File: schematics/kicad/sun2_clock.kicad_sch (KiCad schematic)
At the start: 7 parts, among them U102 74F00, U200 20Mhz, U201 74F74, U203 74F74, U204 74F74, U205 74F74, U313 74F08

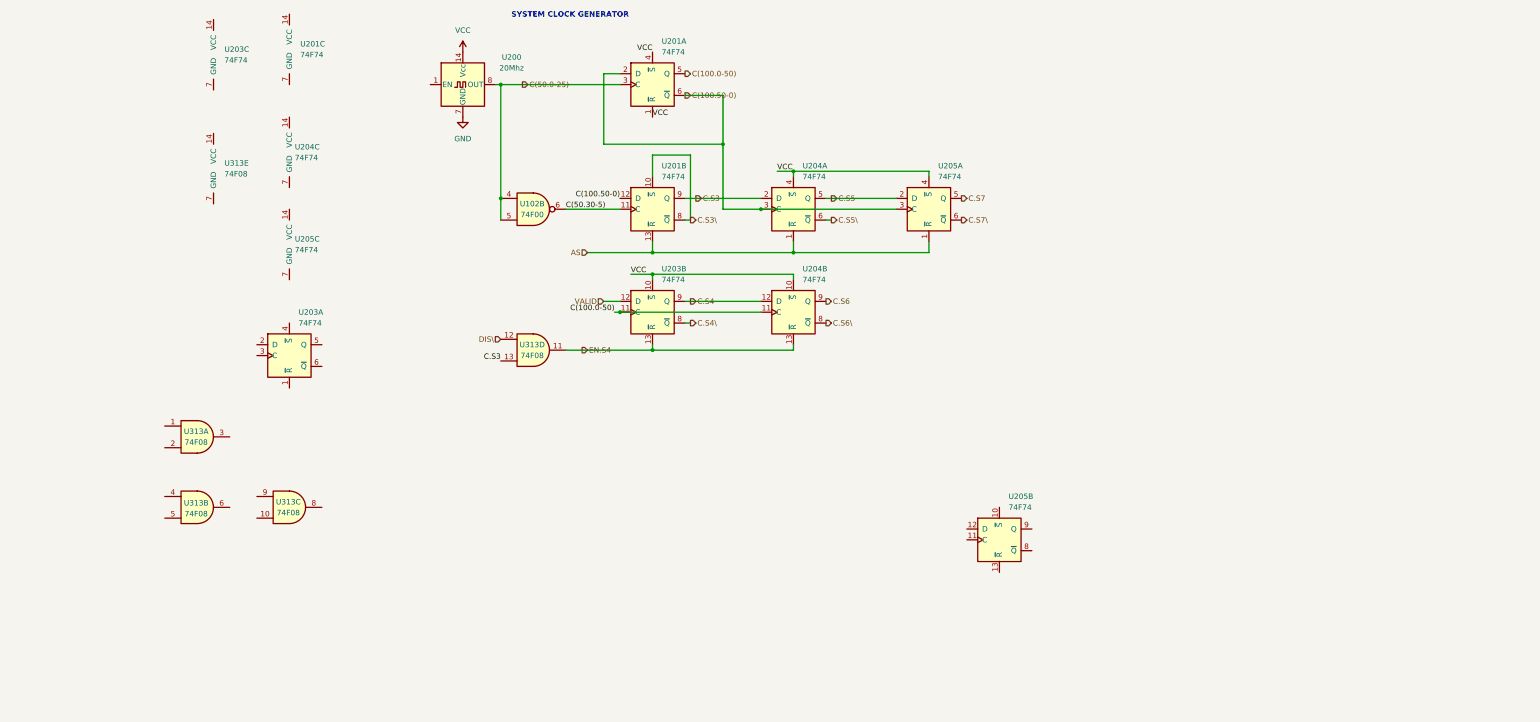
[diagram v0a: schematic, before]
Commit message: Finish page2: Clock, Timers, DVMA
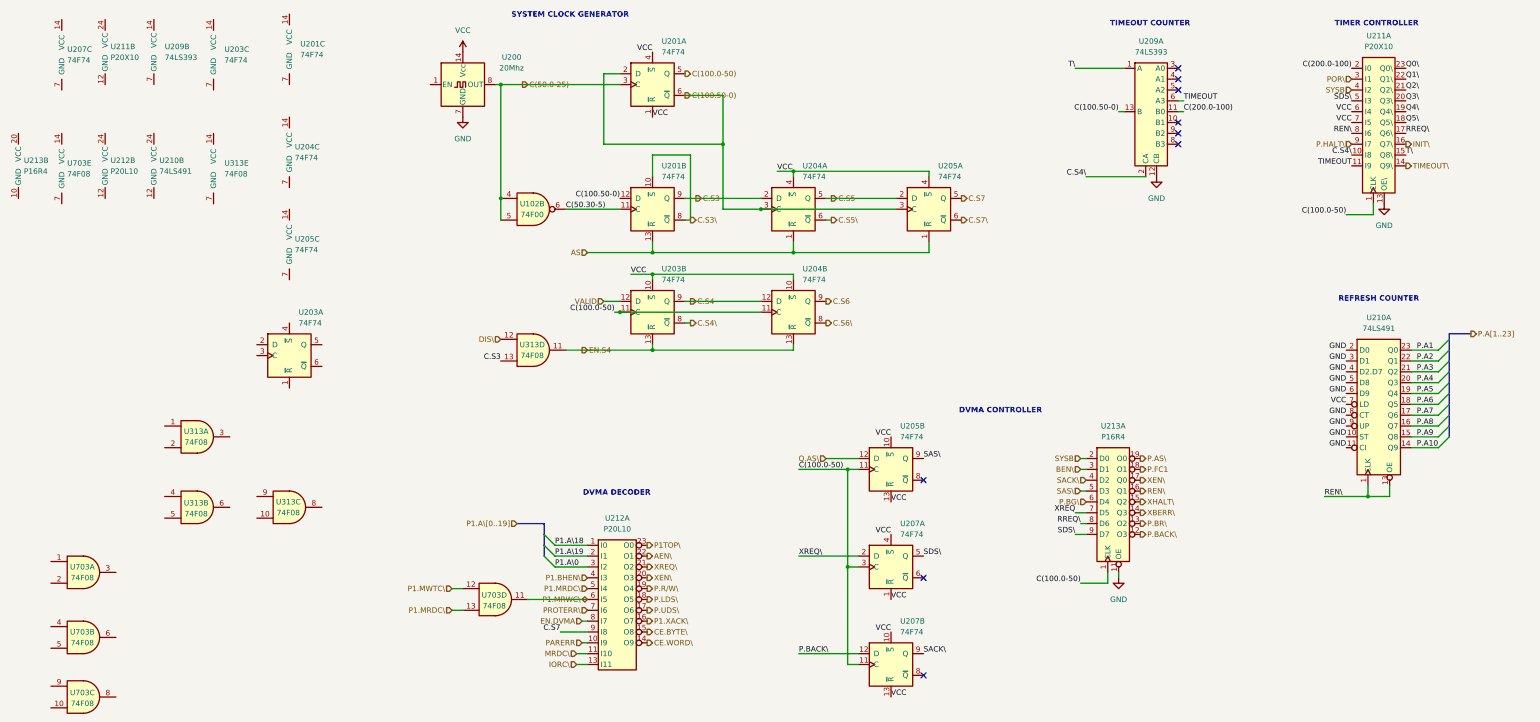
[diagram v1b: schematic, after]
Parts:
- added U207: 74F74, Package_DIP:DIP-14_W7.62mm, symbol sun2:74F74
- added U209: 74LS393, Package_DIP:DIP-14_W7.62mm, symbol sun2:74LS393
- added U210: 74LS491, Package_DIP:DIP-24_W7.62mm, symbol sun2:74LS491
- added U211: P20X10, Package_DIP:DIP-24_W7.62mm, symbol sun2:P20X10
- added U212: P20L10, Package_DIP:DIP-24_W7.62mm, symbol sun2:P20L10
- added U213: P16R4, Package_DIP:DIP-20_W7.62mm, symbol sun2:P16R4
- added U703: 74F08, Package_DIP:DIP-14_W7.62mm, symbol sun2:74F08
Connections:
- net C(100.0-50): now also U205.11 (C), U207.11 (C), U207.3 (C), U211.1 (CLK), U213.1 (CLK)
- net C(100.50-0): now also U209.13 (B)
- net C.S4\: now also U209.2 (CA), U211.10 (I8)
- net C.S7: now also U212.9 (I8)
- net GND: now also U209.12 (CB), U210.10 (ST), U210.11 (CI), U210.2 (D0), U210.3 (D1), U210.4 (D2.D7), U210.5 (D8), U210.6 (D9), U210.8 (CT), U210.9 (UP), U211.13 (OE\), U213.11 (OE)
- net VCC: now also U205.10 (~{S}), U205.13 (~{R}), U207.1 (~{R}), U207.10 (~{S}), U207.13 (~{R}), U207.4 (~{S}), U210.7 (LD), U211.6 (I4), U211.7 (I5)
- net Q.AS\: now reaches U205.12 (D)
- net SAS\: now reaches U205.9 (Q)
- net SAS\: now also U213.5 (D3)
- new net AEN\: U212.22 (O1)
- new net BEN\: U213.3 (D1)
- new net C(200.0-100): U209.11 (B0), U211.2 (I0)
- new net CE.BYTE\: U212.15 (O8)
- new net CE.WORD\: U212.14 (O9)
- new net EN.DVMA: U212.8 (I7)
- new net INIT\: U211.16 (Q7\)
- new net IORC\: U212.13 (I11)
- new net MRDC\: U212.11 (I10)
- new net P.A1: U210.23 (Q0)
- new net P.A10: U210.14 (Q9)
- new net P.A2: U210.22 (Q1)
- new net P.A3: U210.21 (Q2)
- new net P.A4: U210.20 (Q3)
- new net P.A5: U210.19 (Q4)
- new net P.A6: U210.18 (Q5)
- new net P.A7: U210.17 (Q6)
- new net P.A8: U210.16 (Q7)
- new net P.A9: U210.15 (Q8)
- new net P.AS\: U213.19 (O0)
- new net P.BACK\: U207.12 (D), U213.12 (O3)
- new net P.BG\: U213.6 (D4)
- new net P.BR\: U213.13 (O2)
- new net P.FC1: U213.18 (O1)
- new net P.HALT\: U211.9 (I7)
- new net P.LDS\: U212.18 (O5)
- new net P.R/W\: U212.19 (O4)
- new net P.UDS\: U212.17 (O6)
- new net P1.A\0: U212.3 (I2)
- new net P1.A\18: U212.1 (I0)
- new net P1.A\19: U212.2 (I1)
- new net P1.BHEN\: U212.4 (I3)
- new net P1.MRDC\: U212.5 (I4), U703.13
- new net P1.MRWC\: U212.6 (I5), U703.11
- new net P1.MWTC\: U703.12
- new net P1.XACK\: U212.16 (O7)
- new net P1TOP\: U212.23 (O0)
- new net PARERR: U212.10 (I9)
- new net POR\: U211.3 (I1)
- new net PROTERR\: U212.7 (I6)
- new net Q0\: U211.23 (Q0\)
- new net Q1\: U211.22 (Q1\)
- new net Q2\: U211.21 (Q2\)
- new net Q3\: U211.20 (Q3\)
- new net Q4\: U211.19 (Q4\)
- new net Q5\: U211.18 (Q5\)
- new net REN\: U210.1 (CLK), U210.13 (OE), U211.8 (I6), U213.16 (Q1)
- new net RREQ\: U211.17 (Q6\), U213.8 (D6)
- new net SACK\: U207.9 (Q), U213.4 (D2)
- new net SDS\: U207.5 (Q), U211.5 (I3), U213.9 (D7)
- new net SYSB: U211.4 (I2), U213.2 (D0)
- new net TIMEOUT: U209.6 (A3), U211.11 (I9)
- new net TIMEOUT\: U211.14 (Q9\)
- new net T\: U209.1 (A), U211.15 (Q8\)
- new net XBERR\: U213.14 (Q3)
- new net XEN\: U212.20 (O3), U213.17 (Q0)
- new net XHALT\: U213.15 (Q2)
- new net XREQ: U213.7 (D5)
- new net XREQ\: U207.2 (D), U212.21 (O2)
- no-connect marks 0 -> 9
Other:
- note added: "DVMA CONTROLLER"
- note added: "DVMA DECODER"
- note added: "REFRESH COUNTER"
- note added: "TIMEOUT COUNTER"
- note added: "TIMER CONTROLLER"
- moved on the sheet: U205B

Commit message: more mmu work
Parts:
- removed unit 2 of U210
- removed unit 2 of U212
- removed unit 2 of U213
- removed unit 1 of U313
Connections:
- net GND: now also U210.12 (GND), U212.12 (GND), U213.10 (GND)
- net VCC: now also U210.24 (VCC), U212.24 (VCC), U213.20 (VCC)
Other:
- moved on the sheet: U209A, U211A

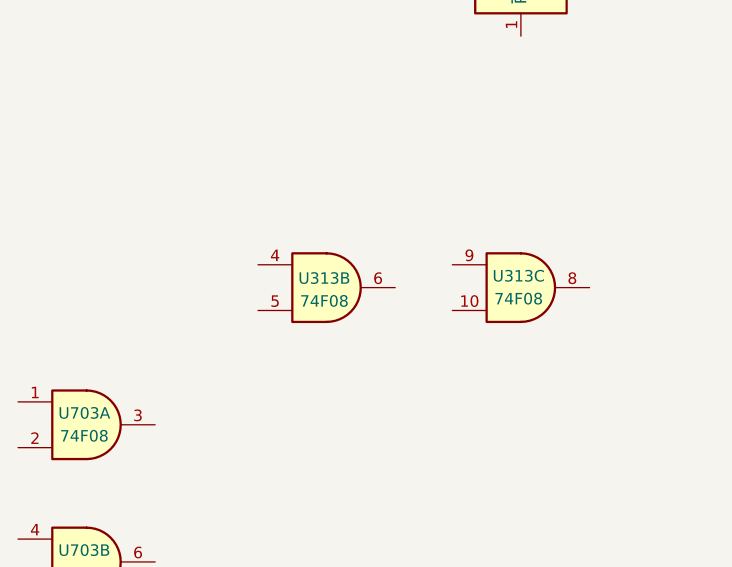
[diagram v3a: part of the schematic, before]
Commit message: Start on rasterop, parity, P2
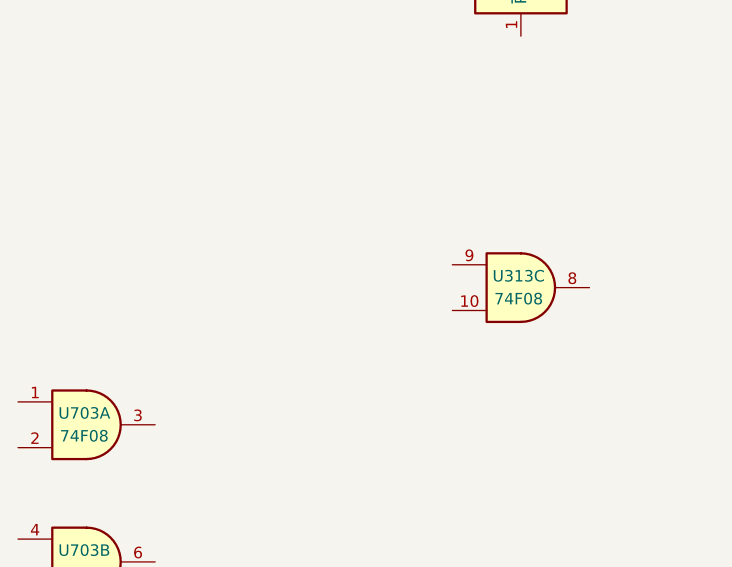
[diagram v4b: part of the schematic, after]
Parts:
- removed unit 2 of U313
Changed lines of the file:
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@@
-	)
-	(symbol
-		(lib_id "sun2:74F08")
-		(at -31.75 135.89 0)
-		(unit 2)
-		(exclude_from_sim no)
-		(in_bom yes)
-		(on_board yes)
-		(dnp no)
-		(property "Reference" "U313"
-			(at -32.004 134.874 0)
-			(effects
-				(font
-					(size 1.27 1.27)
-				)
-			)
-		)
-		(property "Value" "74F08"
-			(at -32.004 137.414 0)
-			(effects
-				(font
-					(size 1.27 1.27)
-				)
-			)
-		)
-		(property "Footprint" "Package_DIP:DIP-14_W7.62mm"
-			(at -31.75 135.89 0)
-			(effects
-				(font
-					(size 1.27 1.27)
-				)
-				(hide yes)
-			)
-		)
-		(property "Datasheet" "https://www.ti.com/lit/ds/symlink/sn74f08.pdf"
-			(at -31.75 135.89 0)
-			(effects
-				(font
-					(size 1.27 1.27)
-				)
-				(hide yes)
-			)
-		)
-		(property "Description" "Quad And2"
-			(at -31.75 135.89 0)
-			(effects
-				(font
-					(size 1.27 1.27)
-				)
-				(hide yes)
-			)
-		)
-		(property "Order Link" "https://www.digikey.com/en/products/detail/texas-instruments/SN74F08N/373669"
-			(at -31.75 135.89 0)
-			(effects
-				(font
-					(size 1.27 1.27)
-				)
-				(hide yes)
-			)
-		)
-		(pin "8"
-		)
-		(pin "6"
-		)
-		(pin "4"
-		)
-		(pin "9"
-		)
-		(pin "1"
-		)
-		(pin "3"
-		)
-		(pin "10"
-		)
-		(pin "5"
-		)
-		(pin "2"
-		)
-		(pin "11"
-		)
-		(pin "14"
-		)
-		(pin "7"
-		)
-		(pin "12"
-		)
-		(pin "13"
-		)
-		(instances
-			(project ""
-				(path "/67ee2072-0b57-4a50-8537-b17b5f651e89/944d560b-cf26-4c91-a0ae-1ed4facdb71d"
-					(reference "U313")
-					(unit 2)
-				)
-			)
-		)
 	)
 	(symbol

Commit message: Serials
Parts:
- removed unit 1 of U203
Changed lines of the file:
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@@
-	)
-	(symbol
-		(lib_id "sun2:74F74")
-		(at -10.16 100.33 0)
-		(unit 1)
-		(exclude_from_sim no)
-		(in_bom yes)
-		(on_board yes)
-		(dnp no)
-		(fields_autoplaced yes)
-		(property "Reference" "U203"
-			(at -8.0167 90.17 0)
-			(effects
-				(font
-					(size 1.27 1.27)
-				)
-				(justify left)
-			)
-		)
-		(property "Value" "74F74"
-			(at -8.0167 92.71 0)
-			(effects
-				(font
-					(size 1.27 1.27)
-				)
-				(justify left)
-			)
-		)
-		(property "Footprint" "Package_DIP:DIP-14_W7.62mm"
-			(at -10.16 100.33 0)
-			(effects
-				(font
-					(size 1.27 1.27)
-				)
-				(hide yes)
-			)
-		)
-		(property "Datasheet" "https://www.ti.com/lit/ds/symlink/sn74f74.pdf"
-			(at -10.16 100.33 0)
-			(effects
-				(font
-					(size 1.27 1.27)
-				)
-				(hide yes)
-			)
-		)
-		(property "Description" "Dual D Flip-flop, Set & Reset"
-			(at -10.16 100.33 0)
-			(effects
-				(font
-					(size 1.27 1.27)
-				)
-				(hide yes)
-			)
-		)
-		(property "Order Link" "https://www.digikey.com/en/products/detail/texas-instruments/SN74F74N/277204"
-			(at -10.16 100.33 0)
-			(effects
-				(font
-					(size 1.27 1.27)
-				)
-				(hide yes)
-			)
-		)
-		(pin "10"
-		)
-		(pin "13"
-		)
-		(pin "11"
-		)
-		(pin "9"
-		)
-		(pin "14"
-		)
-		(pin "8"
-		)
-		(pin "7"
-		)
-		(pin "3"
-		)
-		(pin "2"
-		)
-		(pin "1"
-		)
-		(pin "5"
-		)
-		(pin "12"
-		)
-		(pin "6"
-		)
-		(pin "4"
-		)
-		(instances
-			(project ""
-				(path "/67ee2072-0b57-4a50-8537-b17b5f651e89/944d560b-cf26-4c91-a0ae-1ed4facdb71d"
-					(reference "U203")
-					(unit 1)
-				)
-			)
-		)
 	)
 	(symbol

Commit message: work on addresses and buffers
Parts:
- removed unit 3 of U703
- removed unit 1 of U703
- removed unit 2 of U703
